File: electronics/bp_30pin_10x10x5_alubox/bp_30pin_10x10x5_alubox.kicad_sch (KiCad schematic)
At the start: 8 parts

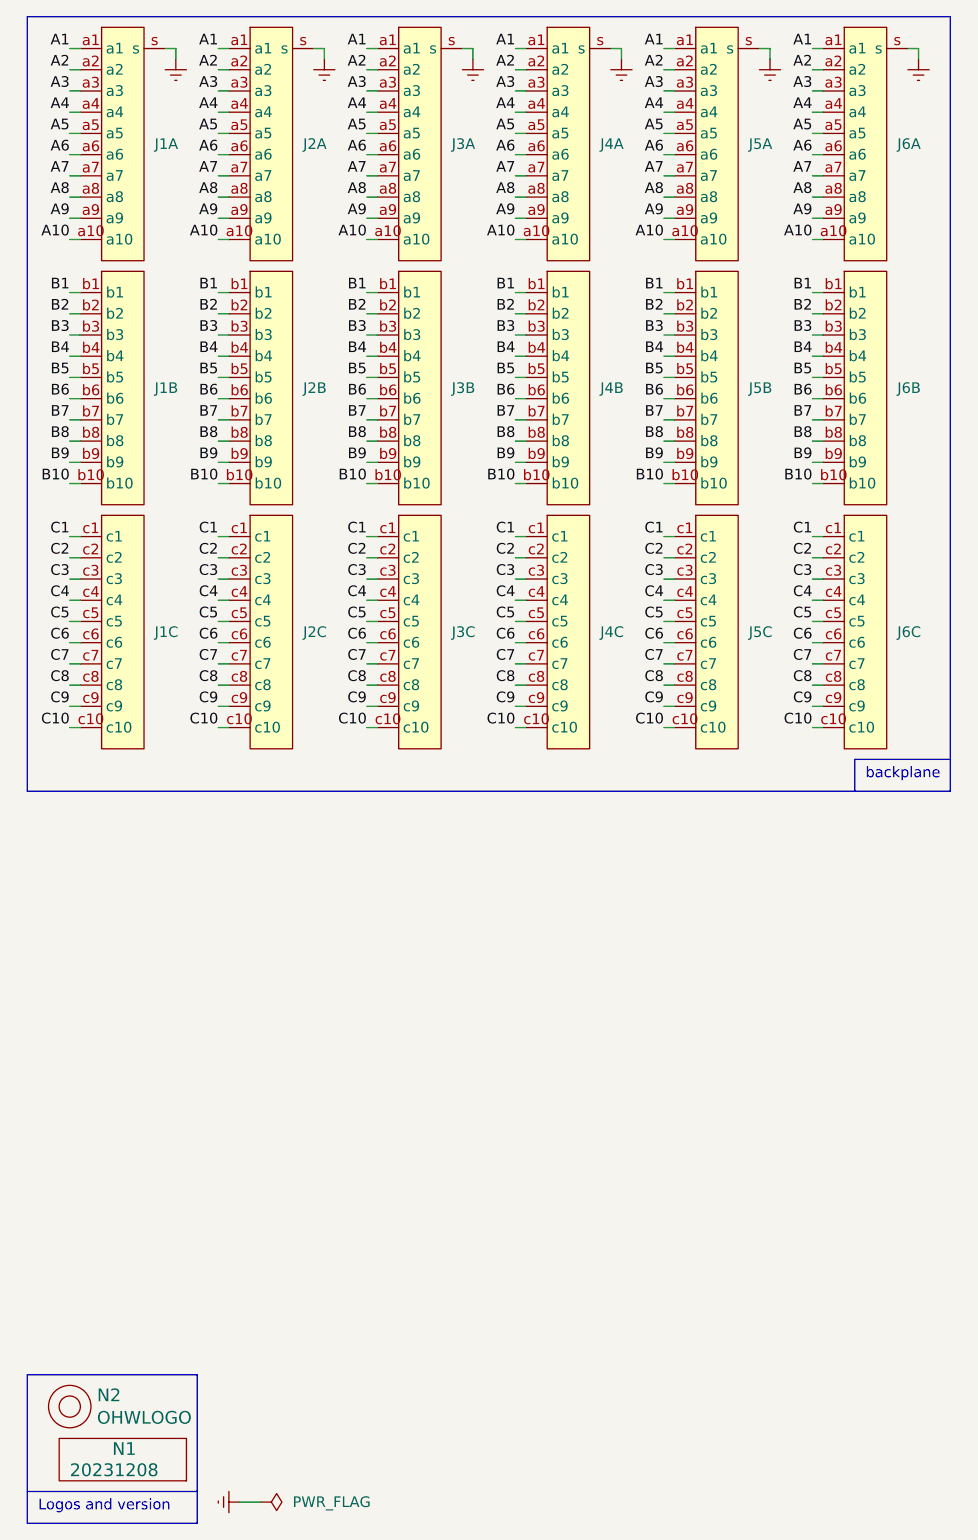
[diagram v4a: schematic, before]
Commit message: removed one connector to give a 16mm pitch for the modules, one module will be a bit small cramped
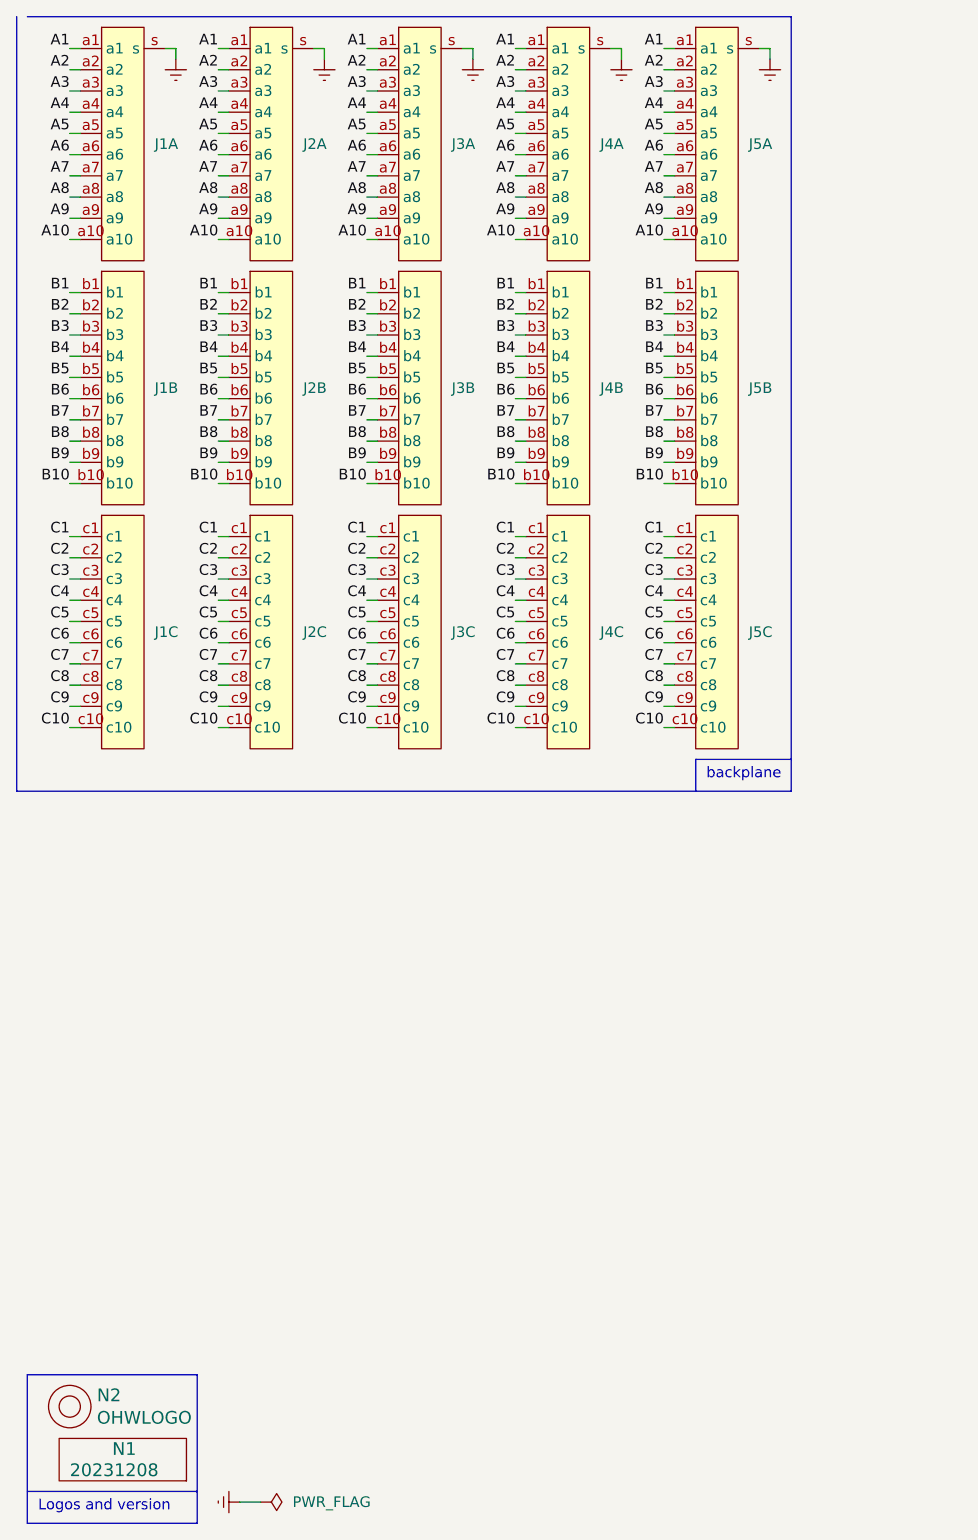
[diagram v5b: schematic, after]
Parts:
- removed J6: ~, SquantorConnectors:DIN41612_R3_3x10_Male_Vertical_THT_shield, symbol SquantorConnectors:DIN41612_03x10_ABC_screws

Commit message: updated backplane to new components
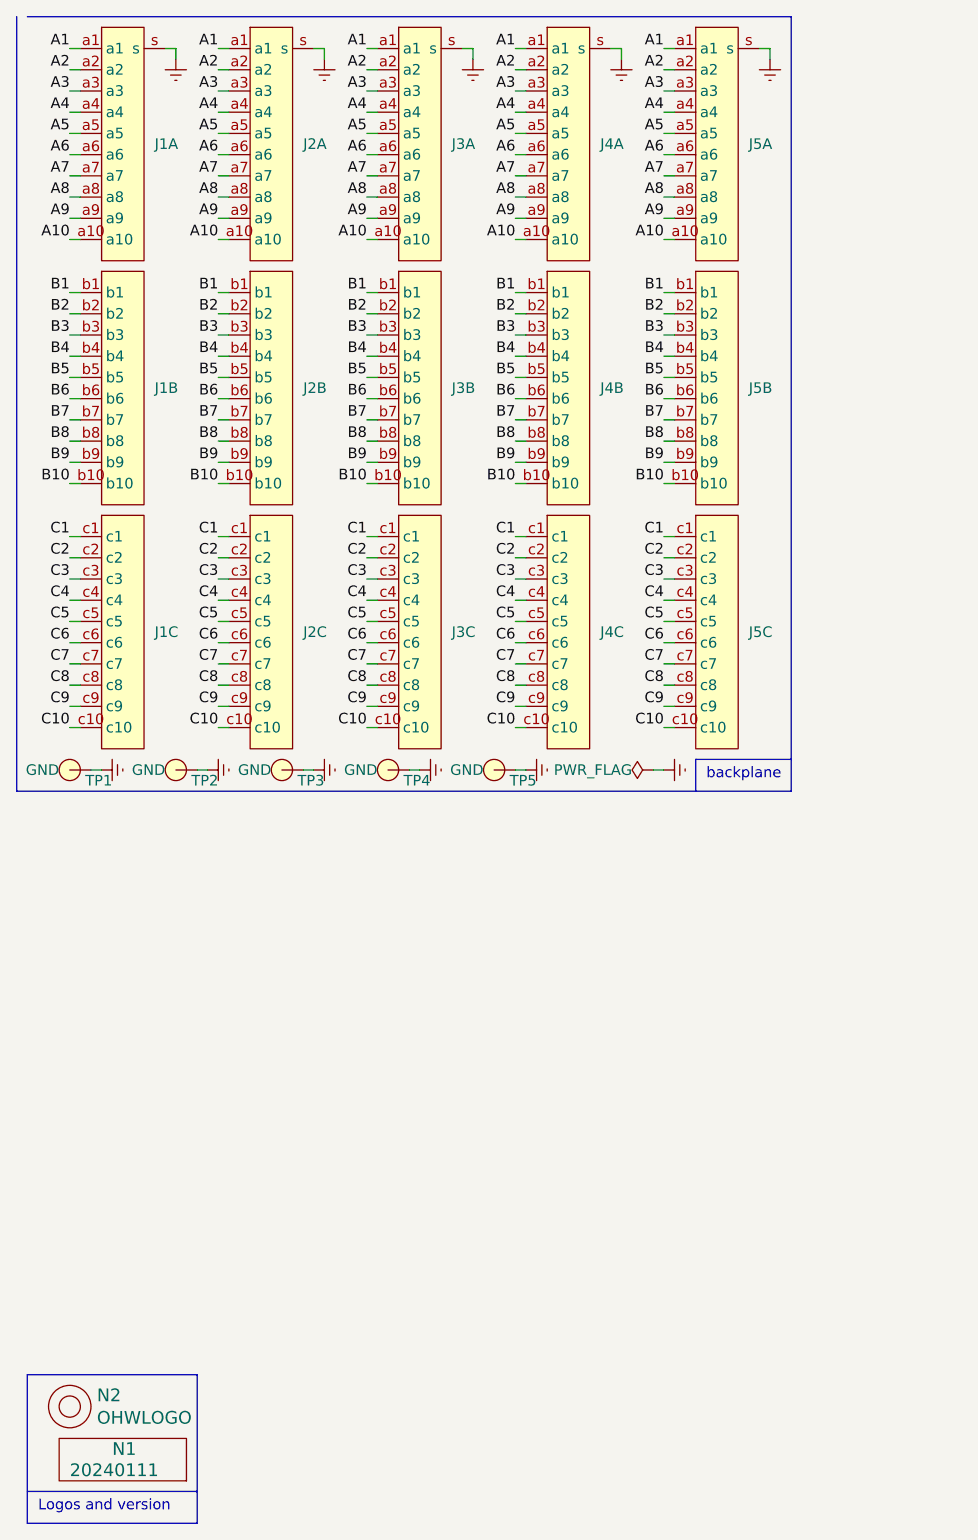
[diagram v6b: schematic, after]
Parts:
- added TP1, TP2, TP3, TP4, TP5: GND, SquantorTestPoints:TestPoint_hole_H05R10, symbol SquantorProto:testpad
- N1: value 20231208 -> 20240111
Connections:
- net Earth: now also TP1.1, TP2.1, TP3.1, TP4.1, TP5.1

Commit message: prepared for production
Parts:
- N1: value 20240111 -> 20240217
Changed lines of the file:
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@@
       (effects (font (size 1.524 1.524)) (justify left))
     )
-    (property "Value" "20240111" (at 20.32 189.23 0)
+    (property "Value" "20240217" (at 20.32 189.23 0)
       (effects (font (size 1.524 1.524)) (justify left))
     )

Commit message: prepared for production
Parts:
- N1: value 20240217 -> 20240218
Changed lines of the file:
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@@
       (effects (font (size 1.524 1.524)) (justify left))
     )
-    (property "Value" "20240217" (at 20.32 189.23 0)
+    (property "Value" "20240218" (at 20.32 189.23 0)
       (effects (font (size 1.524 1.524)) (justify left))
     )
